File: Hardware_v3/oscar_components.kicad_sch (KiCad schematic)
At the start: 71 parts, among them J1 SWD_Header, J10 MIDI_THROUGH, J11 USB_C_Receptacle, J12 Debug_Header, J2 Eurorack_10_pin_power, J3 ChannelC_In, J4 ChannelA_In, J5 ChannelB_In, J6 ChC_Buff_Out, J7 ChA_Buff_Out, J8 ChB_Buff_Out, J9 MIDI_IN, SW1 Reset_Button, SW2 Menu_Button, SW3 Left_Encoder, SW4 Right_Encoder, U1 LT1117-3.3, U2 ILI9341_SPI_Daughterboard, U3 STM32F446RETx, U4 TL074, U5 MCP6004, U6 H11L1, Y1 8MHz

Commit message: Schematic annotation
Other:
- note added: "USART3_RX"
- note added: "USART3_TX"
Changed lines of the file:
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@@
+		)
+	)
+	(text "USART3_TX"
+		(exclude_from_sim no)
+		(at 42.164 98.298 0)
+		(effects
+			(font
+				(size 1.27 1.27)
+			)
 		)
 	)
@@
 		)
 	)
+	(text "USART3_RX"
+		(exclude_from_sim no)
+		(at 42.164 100.838 0)
+		(effects
+			(font
+				(size 1.27 1.27)
+			)
+		)
+	)

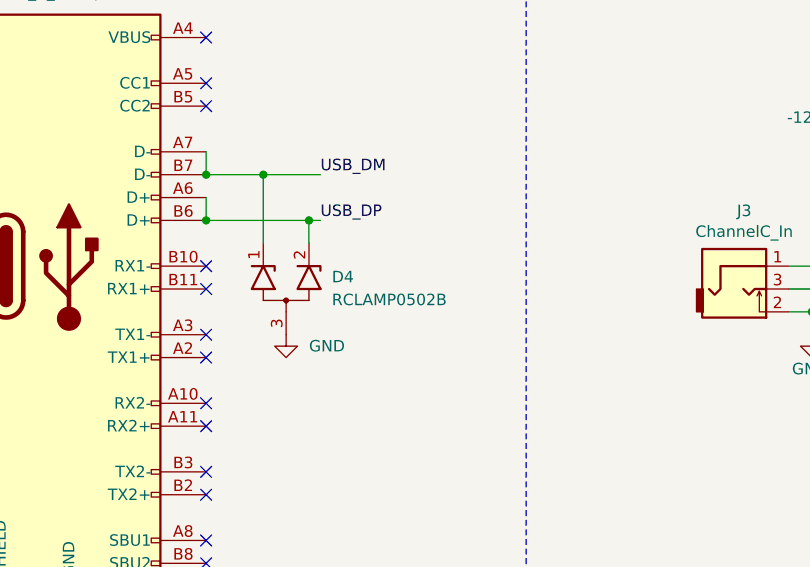
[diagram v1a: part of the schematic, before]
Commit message: New 3.1 daughterboard layout
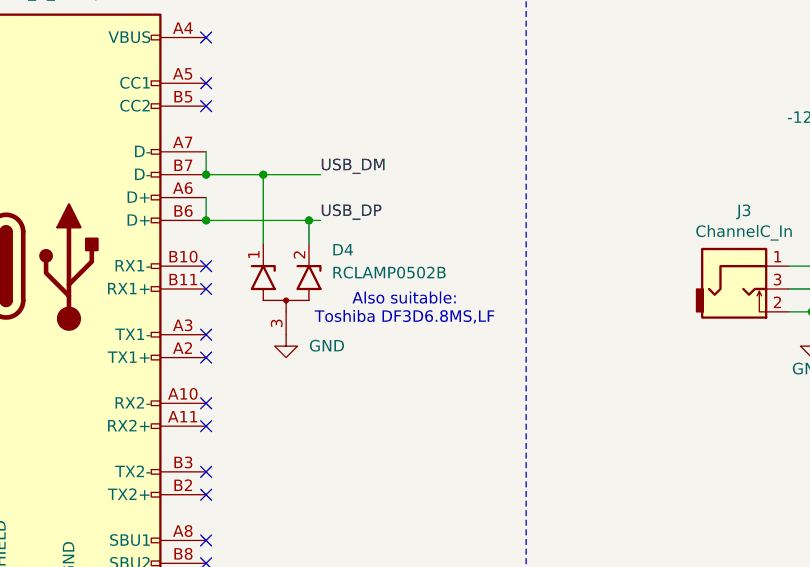
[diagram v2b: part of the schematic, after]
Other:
- note added: "Also suitable: Toshiba DF3D6.8MS,LF"
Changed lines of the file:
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@@
 		)
 	)
+	(text "Also suitable: \nToshiba DF3D6.8MS,LF\n"
+		(exclude_from_sim no)
+		(at 286.258 74.676 0)
+		(effects
+			(font
+				(size 1.27 1.27)
+			)
+		)
+	)
 	(text "Encoders"
 		(exclude_from_sim no)
@@
 		(on_board yes)
 		(dnp no)
-		(fields_autoplaced yes)
 		(property "Reference" "D4"
-			(at 278.13 71.0564 90)
+			(at 278.13 68.072 90)
 			(effects
 				(font
@@
 		)
 		(property "Value" "RCLAMP0502B"
-			(at 278.13 73.5964 90)
+			(at 278.13 70.612 90)
 			(effects
 				(font

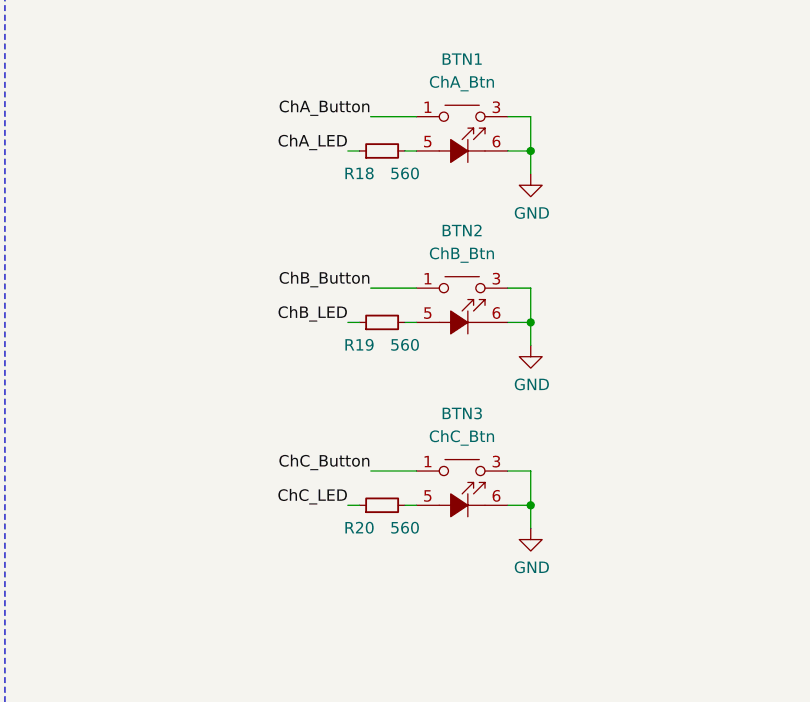
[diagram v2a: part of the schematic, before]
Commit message: Updated LED resistor values
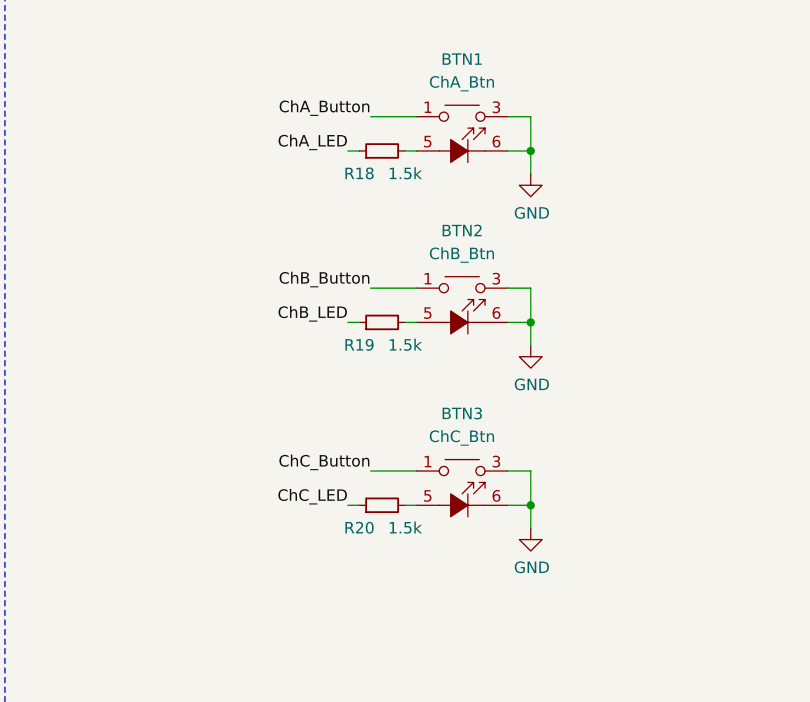
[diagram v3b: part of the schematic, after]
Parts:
- R18, R19, R20: value 560 -> 1.5k
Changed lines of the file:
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@@
 			)
 		)
-		(property "Value" "560"
+		(property "Value" "1.5k"
 			(at 171.45 69.85 90)
 			(effects
@@
 			)
 		)
-		(property "Value" "560"
+		(property "Value" "1.5k"
 			(at 171.45 88.9 90)
 			(effects
@@
 			)
 		)
-		(property "Value" "560"
+		(property "Value" "1.5k"
 			(at 171.45 109.22 90)
 			(effects
